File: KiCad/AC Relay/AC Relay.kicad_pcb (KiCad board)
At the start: 2 copper layers, 49.5 x 49.5 mm, 17 parts, among them J1 Screw_Terminal_01x02, J2 Conn_01x06_Female, J3 Screw_Terminal_01x02, K1 1461492-2, Q1 FDN537N, SW1 SW_Push, U1 BU33SD5WG-TR, U2 ESP-12E, U3 HLK-PM01

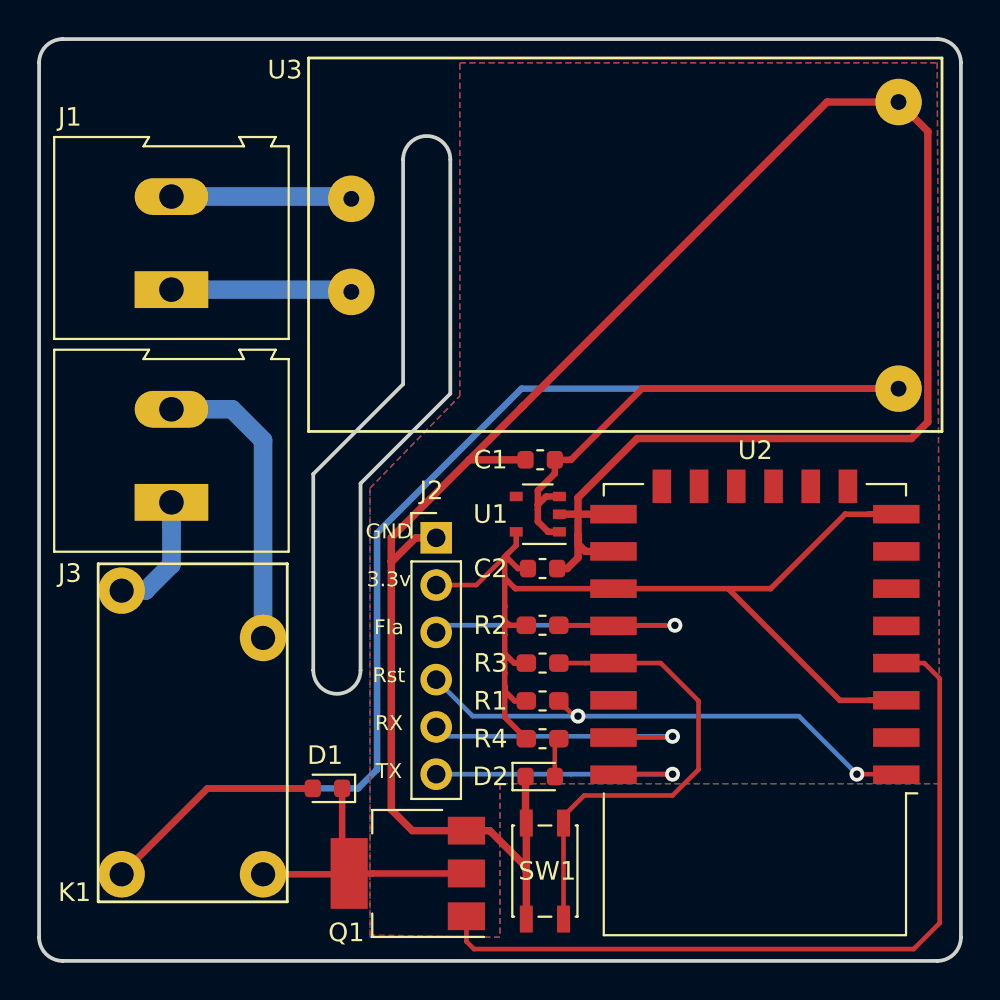
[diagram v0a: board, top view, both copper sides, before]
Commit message: rev: 4 - Change relay to 16 A
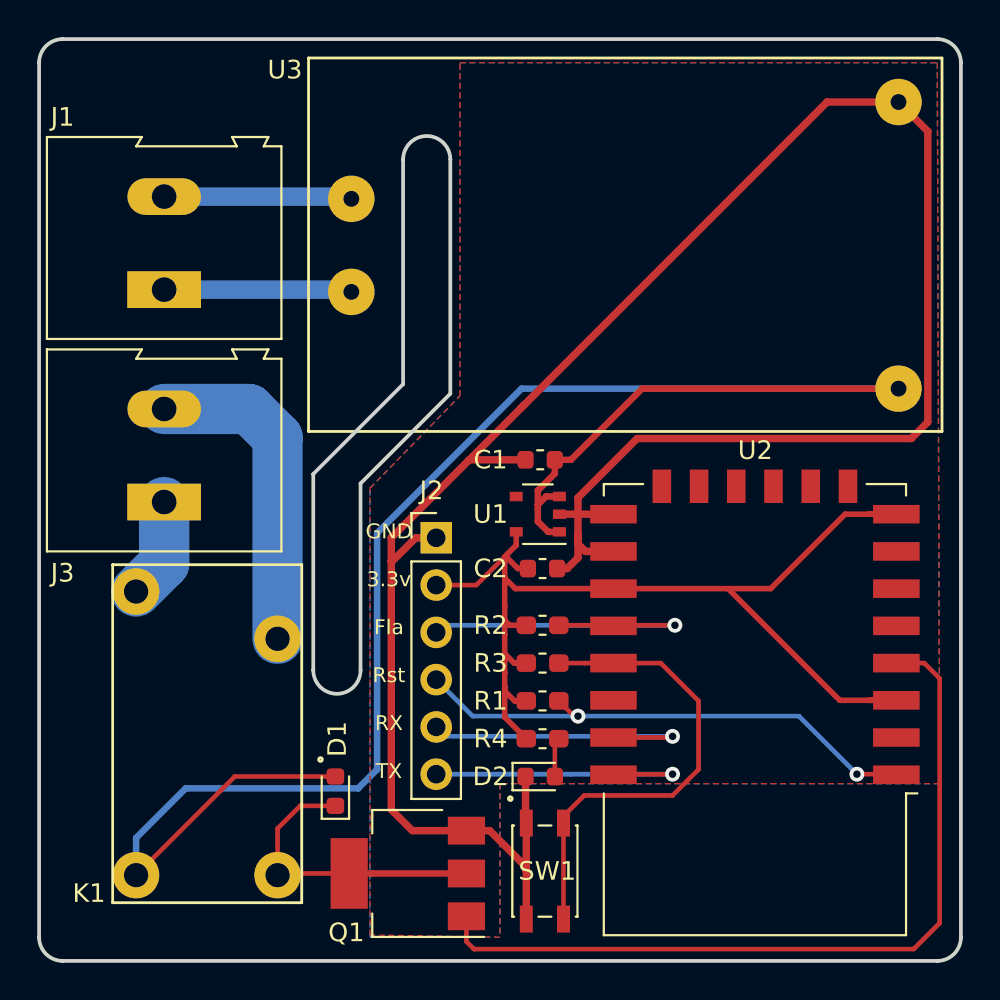
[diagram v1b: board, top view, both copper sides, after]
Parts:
- moved K1 0.78 mm to (82.7, 93.4)
- moved D1 0.45 mm to (84.5, 87.4), turned to 90 degrees
- moved J3 0.39 mm to (75.3, 71.9)
- moved J1 0.39 mm to (75.3, 60.5)
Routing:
- net Net-(J3-Pad2): track 16.2 -> 17.5 mm
- net Net-(D1-Pad1): track 15.7 -> 17.0 mm
- net Net-(J3-Pad1): track 6.60 -> 5.43 mm
- net +5V: track 98.6 -> 99.8 mm
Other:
- net class Default removed
- board text added: "AC Relay - ESP8266 Design by Enrique Gómez CC BY-SA 4.0 enriquegomez.me Rev.: 4 - S/N:"
- board text added: "Relay Max. 16 A"
- board text removed: "AC Relay - ESP8266 Design by Enrique Gómez CC BY-SA 4.0 www.rinconingenieril.es Rev.: 3 - S/N:"
- board text removed: "Relay"
